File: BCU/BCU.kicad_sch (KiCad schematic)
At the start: 6 parts

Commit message: Added some more components
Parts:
- added C1: (no value), symbol SamacSys_Parts:CL10A106KP8NNNC
- added C2: (no value), symbol SamacSys_Parts:CL05A105KA5NQNC
- added C3: (no value), symbol SamacSys_Parts:CL05B104KO5NNNC
- added C4: (no value), symbol SamacSys_Parts:CL05C100JB5NNNC
- added C?: 50V 10PF C0G, CAPC1005X55N, symbol SamacSys_Parts:CL05C100JB5NNNC
- added R1: (no value), symbol SamacSys_Parts:0402WGF1003TCE
- IC1: value (none) -> STM32G474RET6; footprint (none) -> QFP50P1200X1200X160-64N
- IC2: value (none) -> TJA1042T_3,118; footprint (none) -> SOIC127P600X175-8N
- IC3: value (none) -> LM317MDCYR; footprint (none) -> SOT230P700X180-4N
- IC4: value (none) -> LTC6820HUD#PBF; footprint (none) -> QFN50P300X300X80-17N-D
- J1: value (none) -> FTSH-105-01-F-DV-K-P-TR; footprint (none) -> FTSH-105-XX-YYY-DV-K-P-TR
- Y1: value (none) -> NX2520SA-24.000000MHZ-B8; footprint (none) -> NX2520SA24000000MHZB8
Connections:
- net at Y1.1 (X1): now also IC1.5 (PF0-OSC_IN), C?.2
- net GND: now reaches Y1.2 (GND_1)
- net GND: now also Y1.4 (GND_2), C4.1, C?.1, R1.2
- net at Y1.3 (X2): now also IC1.6 (PF1-OSC_OUT), C4.2
- net at IC1.61 (PB8-BOOT0): now also R1.1
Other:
- moved on the sheet: J1, Y1

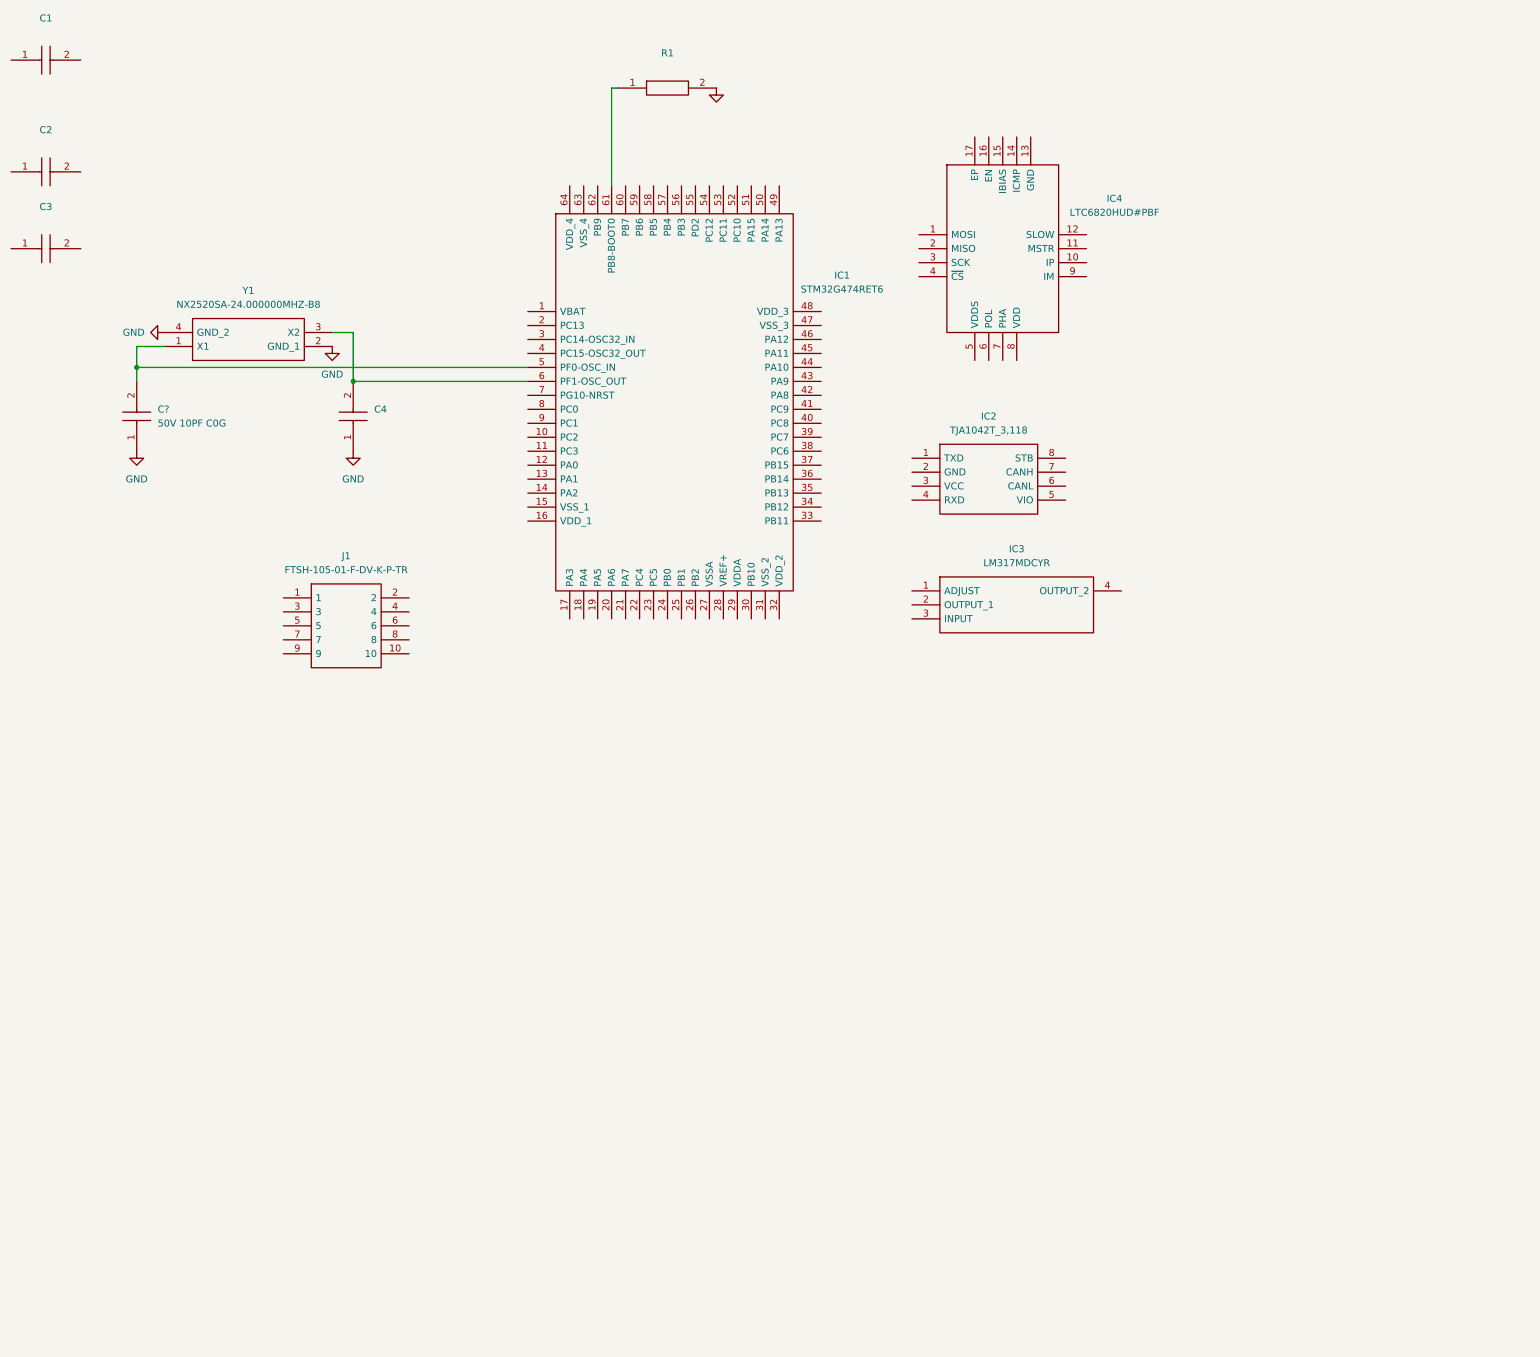
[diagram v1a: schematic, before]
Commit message: Update BCU.kicad_sch
placed and wired a few more symbols
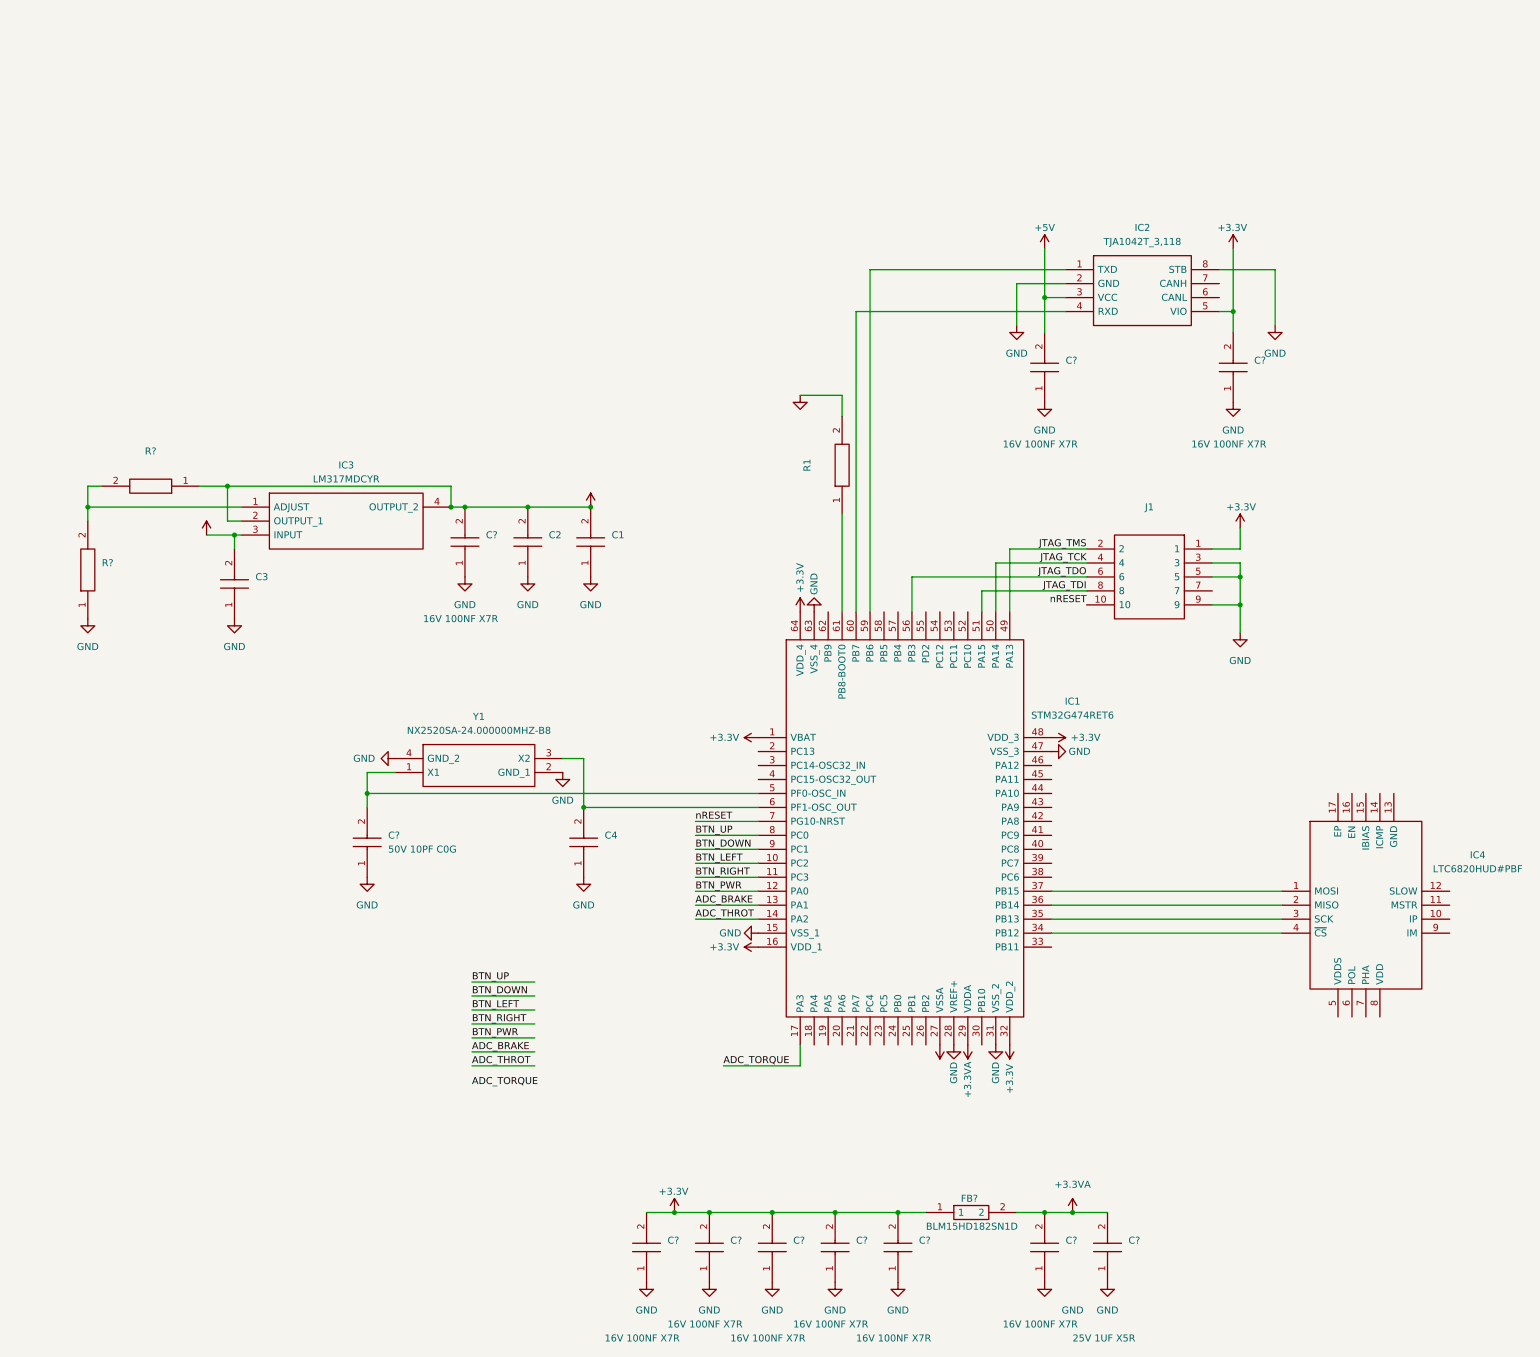
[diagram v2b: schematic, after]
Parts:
- added C? (x9): 16V 100NF X7R, CAPC1005X55N, symbol SamacSys_Parts:CL05B104KO5NNNC
- added C?: 25V 1UF X5R, CAPC1005X60N, symbol SamacSys_Parts:CL05A105KA5NQNC
- added FB?: BLM15HD182SN1D, NFZ15SG152SN10B, symbol SamacSys_Parts:BLM15HD182SN1D
- added R?: (no value), symbol SamacSys_Parts:0402WGF1002TCE
- added R?: (no value), symbol SamacSys_Parts:0402WGF8201TCE
- J1: value FTSH-105-01-F-DV-K-P-TR -> (none)
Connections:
- net GND: now also C1.1, C2.1, C3.1, IC1.15 (VSS_1), IC1.28 (VREF+), IC1.31 (VSS_2), IC1.47 (VSS_3), IC1.63 (VSS_4), IC2.2 (GND), IC2.8 (STB), J1.3, J1.5, J1.9, C?.1, C?.1, C?.1, C?.1, C?.1, C?.1, C?.1, C?.1, C?.1, C?.1, R?.1
- net +3V3: now reaches J1.1
- net +3V3: now also C1.2, C2.2, IC1.1 (VBAT), IC1.16 (VDD_1), IC1.32 (VDD_2), IC1.48 (VDD_3), IC1.64 (VDD_4), IC2.5 (VIO), IC3.2 (OUTPUT_1), IC3.4 (OUTPUT_2), C?.2, C?.2, C?.2, C?.2, C?.2, C?.2, C?.2, FB?.1, R?.1
- net nRESET: now reaches J1.10
- net nRESET: now also IC1.7 (PG10-NRST)
- net JTAG_TMS: now reaches J1.2
- net JTAG_TMS: now also IC1.49 (PA13)
- net JTAG_TCK: now reaches J1.4
- net JTAG_TCK: now also IC1.50 (PA14)
- net JTAG_TDO: now reaches J1.6
- net JTAG_TDO: now also IC1.56 (PB3)
- net JTAG_TDI: now reaches J1.8
- net JTAG_TDI: now also IC1.51 (PA15)
- net at IC2.1 (TXD): now also IC1.59 (PB6)
- net +5V: now reaches IC2.3 (VCC)
- net +5V: now also C3.2, IC3.3 (INPUT), C?.2
- net at IC2.4 (RXD): now also IC1.60 (PB7)
- net BTN_LEFT: now reaches IC1.10 (PC2)
- net BTN_RIGHT: now reaches IC1.11 (PC3)
- net BTN_PWR: now reaches IC1.12 (PA0)
- net ADC_BRAKE: now reaches IC1.13 (PA1)
- net ADC_THROT: now reaches IC1.14 (PA2)
- net ADC_TORQUE: now reaches IC1.17 (PA3)
- net +3.3VA: now reaches IC1.27 (VSSA)
- net +3.3VA: now also IC1.29 (VDDA), C?.2, C?.2, FB?.2
- net at IC1.34 (PB12): now also IC4.4 (~{CS})
- net at IC1.35 (PB13): now also IC4.3 (SCK)
- net at IC1.36 (PB14): now also IC4.2 (MISO)
- net at IC1.37 (PB15): now also IC4.1 (MOSI)
- net BTN_UP: now reaches IC1.8 (PC0)
- net BTN_DOWN: now reaches IC1.9 (PC1)
- net at IC3.1 (ADJUST): now also R?.2, R?.2
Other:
- moved on the sheet: C1, C2, C3, C4, C?, IC1, IC2, IC3, IC4, J1, R1, Y1

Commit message: Update BCU.kicad_sch
wip
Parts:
- added C?: (no value), symbol SamacSys_Parts:CL05B104KB54PNC
- added C?: (no value), symbol SamacSys_Parts:GRM21BR61H106KE43L
- added C? (x4): 16V 100NF X7R, CAPC1005X55N, symbol SamacSys_Parts:CL05B104KO5NNNC
- added C? (x3): 10V 10UF X5R, CAPC1608X90N, symbol SamacSys_Parts:CL10A106KP8NNNC
- added C?: 25V 1UF X5R, CAPC1005X60N, symbol SamacSys_Parts:CL05A105KA5NQNC
- added D?: (no value), symbol SamacSys_Parts:MBR140SFT1G
- added H?: (no value), symbol Mechanical:MountingHole
- added H? (x3): MountingHole, MountingHole:MountingHole_2.2mm_M2, symbol Mechanical:MountingHole
- added IC?: (no value), symbol SamacSys_Parts:LM2842YQMK_NOPB
- added J? (x3): (no value), symbol SamacSys_Parts:SM04B-PASS-TBT_LF__SN_
- added J?: (no value), symbol Connector:Conn_01x07_Male
- added J?: (no value), symbol Connector:USB_C_Receptacle_USB2.0
- added L?: (no value), symbol SamacSys_Parts:CBC3225T680KRV
- added R? (x2): (no value), symbol SamacSys_Parts:0402WGF8201TCE
- added R? (x3): 51R 1% 1/16W 0402, RESC1005X40N, symbol SamacSys_Parts:0402WGF8201TCE
- added R?: 8.2K 1% 1/16W 0402, RESC1005X40N, symbol SamacSys_Parts:0402WGF8201TCE
- added S? (x4): TS-1101-C-W, TS1101CW, symbol SamacSys_Parts:TS-1101-C-W
- added S?: (no value), symbol SamacSys_Parts:TS-1101-C-W
- added T?: (no value), symbol SamacSys_Parts:PE-68386NLT
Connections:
- net +3V3: now also J?.1 (Pin_1)
- net +5V: now also C?.2, C?.2, C?.2, C?.2, C?.2, D?.1, L?.2, R?.1
- net GND: now also C?.1, C?.1, C?.1, C?.1, C?.1, C?.1, C?.1, D?.2, IC?.2 (GND), J?.2 (Pin_2), R?.2
- net at IC2.6 (CANL): now also J?.2, R?.1
- net at IC2.7 (CANH): now also J?.1, R?.1
- net OLED_CS: now reaches IC1.18 (PA4)
- net OLED_CS: now also J?.5 (Pin_5)
- net OLED_CLK: now reaches IC1.19 (PA5)
- net OLED_CLK: now also J?.4 (Pin_4)
- net OLED_DIN: now reaches IC1.21 (PA7)
- net OLED_DIN: now also J?.3 (Pin_3)
- net OLED_RST: now reaches IC1.22 (PC4)
- net OLED_RST: now also J?.7 (Pin_7)
- net OLED_DC: now reaches IC1.30 (PB10)
- net OLED_DC: now also J?.6 (Pin_6)
- net at IC4.10 (IP): now also R?.1, T?.1 (PRI_1)
- net at IC4.9 (IM): now also R?.1, T?.2 (PRI_2)
- new net: C?.1, IC?.6 (SW), L?.1
- new net: C?.2, IC?.1 (CB)
- new net: C?.2, R?.2, R?.2 (x2)
- new net: J?.2, T?.3 (SEC_1)
- new net: J?.1, T?.4 (SEC_2)
- new net: IC?.3 (FB), R?.1, R?.2
- new net: J?.A1 (GND), J?.A12 (GND), J?.B1 (GND), J?.B12 (GND)
- new net: J?.A4 (VBUS), J?.A9 (VBUS), J?.B4 (VBUS), J?.B9 (VBUS)
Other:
- note added: "Battery connection"
- note added: "Check if part from JLC will fit https://datasheet.lcsc.com/lcsc/2108131730_Korean-Hroparts-Elec-TYPE-C-31-M-12_C165948.pdf"
- note added: "DOWN button"
- note added: "LEFT button"
- note added: "OLED interface"
- note added: "Power button"
- note added: "RIGHT button"
- note added: "Torque sensor"
- note added: "UP button"
- note added: "VESC connection"
